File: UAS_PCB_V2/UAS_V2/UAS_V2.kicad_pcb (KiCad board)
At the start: 2 copper layers, 50.8 x 50.8 mm, 2 parts

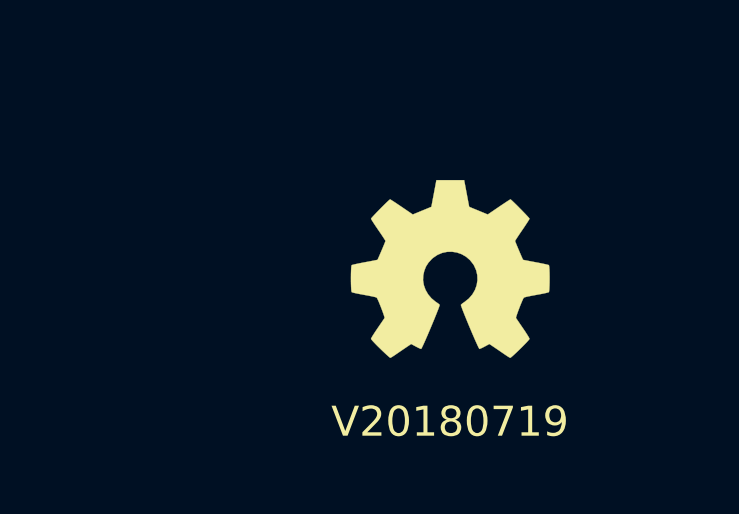
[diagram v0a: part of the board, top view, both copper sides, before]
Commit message: trace changes and fill for teensy pcb
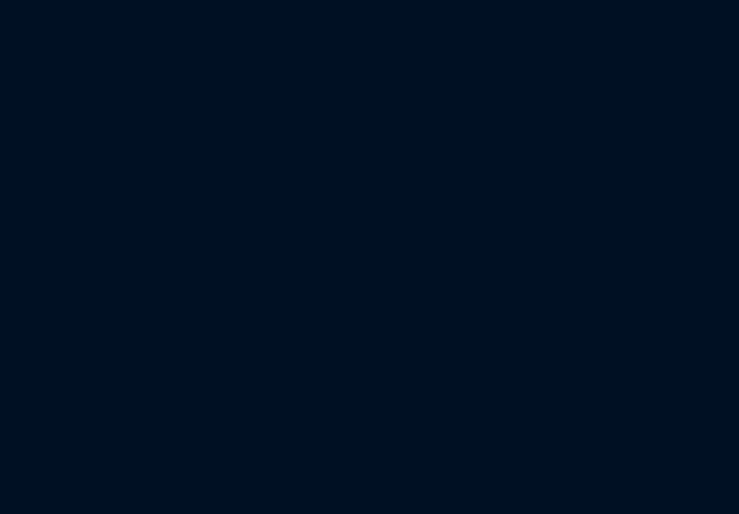
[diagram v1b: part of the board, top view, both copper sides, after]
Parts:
- removed N1: OHWLOGO, Symbols:OSHW-Symbol_6.7x6mm_SilkScreen
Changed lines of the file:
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@@
     (tracks 0)
     (zones 0)
-    (modules 2)
+    (modules 1)
     (nets 1)
   )
@@
     (uvia_drill 0.3)
   )
-  (module Symbols:OSHW-Symbol_6.7x6mm_SilkScreen (layer F.Cu)
-    (at 167.64 170.18)
-    (descr "Open Source Hardware Symbol")
-    (tags "Logo Symbol OSHW")
-    (attr virtual)
-    (fp_text reference N1 (at 0 -6.35) (layer F.SilkS) hide
-      (effects (font (size 1 1) (thickness 0.15)))
-    )
-    (fp_text value OHWLOGO (at 0 -8.89) (layer F.Fab) hide
-      (effects (font (size 1 1) (thickness 0.15)))
-    )
-    (fp_poly (pts (xy 0.555814 -2.531069) (xy 0.639635 -2.086445) (xy 0.94892 -1.958947) (xy 1.258206 -1.831449)
-      (xy 1.629246 -2.083754) (xy 1.733157 -2.154004) (xy 1.827087 -2.216728) (xy 1.906652 -2.269062)
-      (xy 1.96747 -2.308143) (xy 2.005157 -2.331107) (xy 2.015421 -2.336058) (xy 2.03391 -2.323324)
-      (xy 2.07342 -2.288118) (xy 2.129522 -2.234938) (xy 2.197787 -2.168282) (xy 2.273786 -2.092646)
-      (xy 2.353092 -2.012528) (xy 2.431275 -1.932426) (xy 2.503907 -1.856836) (xy 2.566559 -1.790255)
-      (xy 2.614803 -1.737182) (xy 2.64421 -1.702113) (xy 2.651241 -1.690377) (xy 2.641123 -1.66874)
-      (xy 2.612759 -1.621338) (xy 2.569129 -1.552807) (xy 2.513218 -1.467785) (xy 2.448006 -1.370907)
-      (xy 2.410219 -1.31565) (xy 2.341343 -1.214752) (xy 2.28014 -1.123701) (xy 2.229578 -1.04703)
-      (xy 2.192628 -0.989272) (xy 2.172258 -0.954957) (xy 2.169197 -0.947746) (xy 2.176136 -0.927252)
-      (xy 2.195051 -0.879487) (xy 2.223087 -0.811168) (xy 2.257391 -0.729011) (xy 2.295109 -0.63973)
-      (xy 2.333387 -0.550042) (xy 2.36937 -0.466662) (xy 2.400206 -0.396306) (xy 2.423039 -0.34569)
-      (xy 2.435017 -0.321529) (xy 2.435724 -0.320578) (xy 2.454531 -0.315964) (xy 2.504618 -0.305672)
-      (xy 2.580793 -0.290713) (xy 2.677865 -0.272099) (xy 2.790643 -0.250841) (xy 2.856442 -0.238582)
-      (xy 2.97695 -0.215638) (xy 3.085797 -0.193805) (xy 3.177476 -0.174278) (xy 3.246481 -0.158252)
-      (xy 3.287304 -0.146921) (xy 3.295511 -0.143326) (xy 3.303548 -0.118994) (xy 3.310033 -0.064041)
-      (xy 3.31497 0.015108) (xy 3.318364 0.112026) (xy 3.320218 0.220287) (xy 3.320538 0.333465)
-      (xy 3.319327 0.445135) (xy 3.31659 0.548868) (xy 3.312331 0.638241) (xy 3.306555 0.706826)
-      (xy 3.299267 0.748197) (xy 3.294895 0.75681) (xy 3.268764 0.767133) (xy 3.213393 0.781892)
-      (xy 3.136107 0.799352) (xy 3.04423 0.81778) (xy 3.012158 0.823741) (xy 2.857524 0.852066)
-      (xy 2.735375 0.874876) (xy 2.641673 0.89308) (xy 2.572384 0.907583) (xy 2.523471 0.919292)
-      (xy 2.490897 0.929115) (xy 2.470628 0.937956) (xy 2.458626 0.946724) (xy 2.456947 0.948457)
-      (xy 2.440184 0.976371) (xy 2.414614 1.030695) (xy 2.382788 1.104777) (xy 2.34726 1.191965)
-      (xy 2.310583 1.285608) (xy 2.275311 1.379052) (xy 2.243996 1.465647) (xy 2.219193 1.53874)
-      (xy 2.203454 1.591678) (xy 2.199332 1.617811) (xy 2.199676 1.618726) (xy 2.213641 1.640086)
-      (xy 2.245322 1.687084) (xy 2.291391 1.754827) (xy 2.348518 1.838423) (xy 2.413373 1.932982)
-      (xy 2.431843 1.959854) (xy 2.497699 2.057275) (xy 2.55565 2.146163) (xy 2.602538 2.221412)
-      (xy 2.635207 2.27792) (xy 2.6505 2.310581) (xy 2.651241 2.314593) (xy 2.638392 2.335684)
-      (xy 2.602888 2.377464) (xy 2.549293 2.435445) (xy 2.482171 2.505135) (xy 2.406087 2.582045)
-      (xy 2.325604 2.661683) (xy 2.245287 2.739561) (xy 2.169699 2.811186) (xy 2.103405 2.87207)
-      (xy 2.050969 2.917721) (xy 2.016955 2.94365) (xy 2.007545 2.947883) (xy 1.985643 2.937912)
-      (xy 1.9408 2.91102) (xy 1.880321 2.871736) (xy 1.833789 2.840117) (xy 1.749475 2.782098)
-      (xy 1.649626 2.713784) (xy 1.549473 2.645579) (xy 1.495627 2.609075) (xy 1.313371 2.4858)
-      (xy 1.160381 2.56852) (xy 1.090682 2.604759) (xy 1.031414 2.632926) (xy 0.991311 2.648991)
-      (xy 0.981103 2.651226) (xy 0.968829 2.634722) (xy 0.944613 2.588082) (xy 0.910263 2.515609)
-      (xy 0.867588 2.421606) (xy 0.818394 2.310374) (xy 0.76449 2.186215) (xy 0.707684 2.053432)
-      (xy 0.649782 1.916327) (xy 0.592593 1.779202) (xy 0.537924 1.646358) (xy 0.487584 1.522098)
-      (xy 0.44338 1.410725) (xy 0.407119 1.316539) (xy 0.380609 1.243844) (xy 0.365658 1.196941)
-      (xy 0.363254 1.180833) (xy 0.382311 1.160286) (xy 0.424036 1.126933) (xy 0.479706 1.087702)
-      (xy 0.484378 1.084599) (xy 0.628264 0.969423) (xy 0.744283 0.835053) (xy 0.83143 0.685784)
-      (xy 0.888699 0.525913) (xy 0.915086 0.359737) (xy 0.909585 0.191552) (xy 0.87119 0.025655)
-      (xy 0.798895 -0.133658) (xy 0.777626 -0.168513) (xy 0.666996 -0.309263) (xy 0.536302 -0.422286)
-      (xy 0.390064 -0.506997) (xy 0.232808 -0.562806) (xy 0.069057 -0.589126) (xy -0.096667 -0.58537)
-      (xy -0.259838 -0.55095) (xy -0.415935 -0.485277) (xy -0.560433 -0.387765) (xy -0.605131 -0.348187)
-      (xy -0.718888 -0.224297) (xy -0.801782 -0.093876) (xy -0.858644 0.052315) (xy -0.890313 0.197088)
-      (xy -0.898131 0.35986) (xy -0.872062 0.52344) (xy -0.814755 0.682298) (xy -0.728856 0.830906)
-      (xy -0.617014 0.963735) (xy -0.481877 1.075256) (xy -0.464117 1.087011) (xy -0.40785 1.125508)
-      (xy -0.365077 1.158863) (xy -0.344628 1.18016) (xy -0.344331 1.180833) (xy -0.348721 1.203871)
-      (xy -0.366124 1.256157) (xy -0.394732 1.33339) (xy -0.432735 1.431268) (xy -0.478326 1.545491)
-      (xy -0.529697 1.671758) (xy -0.585038 1.805767) (xy -0.642542 1.943218) (xy -0.700399 2.079808)
-      (xy -0.756802 2.211237) (xy -0.809942 2.333205) (xy -0.85801 2.441409) (xy -0.899199 2.531549)
-      (xy -0.931699 2.599323) (xy -0.953703 2.64043) (xy -0.962564 2.651226) (xy -0.98964 2.642819)
-      (xy -1.040303 2.620272) (xy -1.105817 2.587613) (xy -1.141841 2.56852) (xy -1.294832 2.4858)
-      (xy -1.477088 2.609075) (xy -1.570125 2.672228) (xy -1.671985 2.741727) (xy -1.767438 2.807165)
-      (xy -1.81525 2.840117) (xy -1.882495 2.885273) (xy -1.939436 2.921057) (xy -1.978646 2.942938)
-      (xy -1.991381 2.947563) (xy -2.009917 2.935085) (xy -2.050941 2.900252) (xy -2.110475 2.846678)
-      (xy -2.184542 2.777983) (xy -2.269165 2.697781) (xy -2.322685 2.646286) (xy -2.416319 2.554286)
-      (xy -2.497241 2.471999) (xy -2.562177 2.402945) (xy -2.607858 2.350644) (xy -2.631011 2.318616)
-      (xy -2.633232 2.312116) (xy -2.622924 2.287394) (xy -2.594439 2.237405) (xy -2.550937 2.167212)
-      (xy -2.495577 2.081875) (xy -2.43152 1.986456) (xy -2.413303 1.959854) (xy -2.346927 1.863167)
-      (xy -2.287378 1.776117) (xy -2.237984 1.703595) (xy -2.202075 1.650493) (xy -2.182981 1.621703)
-      (xy -2.181136 1.618726) (xy -2.183895 1.595782) (xy -2.198538 1.545336) (xy -2.222513 1.474041)
-      (xy -2.253266 1.388547) (xy -2.288244 1.295507) (xy -2.324893 1.201574) (xy -2.360661 1.113399)
-      (xy -2.392994 1.037634) (xy -2.419338 0.980931) (xy -2.437142 0.949943) (xy -2.438407 0.948457)
-      (xy -2.449294 0.939601) (xy -2.467682 0.930843) (xy -2.497606 0.921277) (xy -2.543103 0.909996)
-      (xy -2.608209 0.896093) (xy -2.696961 0.878663) (xy -2.813393 0.856798) (xy -2.961542 0.829591)
-      (xy -2.993618 0.823741) (xy -3.088686 0.805374) (xy -3.171565 0.787405) (xy -3.23493 0.771569)
-      (xy -3.271458 0.7596) (xy -3.276356 0.75681) (xy -3.284427 0.732072) (xy -3.290987 0.67679)
-      (xy -3.296033 0.597389) (xy -3.299559 0.500296) (xy -3.301561 0.391938) (xy -3.302036 0.27874)
-      (xy -3.300977 0.167128) (xy -3.298382 0.063529) (xy -3.294246 -0.025632) (xy -3.288563 -0.093928)
-      (xy -3.281331 -0.134934) (xy -3.276971 -0.143326) (xy -3.252698 -0.151792) (xy -3.197426 -0.165565)
-      (xy -3.116662 -0.18345) (xy -3.015912 -0.204252) (xy -2.900683 -0.226777) (xy -2.837902 -0.238582)
-      (xy -2.718787 -0.260849) (xy -2.612565 -0.281021) (xy -2.524427 -0.298085) (xy -2.459566 -0.311031)
-      (xy -2.423174 -0.318845) (xy -2.417184 -0.320578) (xy -2.407061 -0.34011) (xy -2.385662 -0.387157)
-      (xy -2.355839 -0.454997) (xy -2.320445 -0.536909) (xy -2.282332 -0.626172) (xy -2.244353 -0.716065)
-      (xy -2.20936 -0.799865) (xy -2.180206 -0.870853) (xy -2.159743 -0.922306) (xy -2.150823 -0.947503)
-      (xy -2.150657 -0.948604) (xy -2.160769 -0.968481) (xy -2.189117 -1.014223) (xy -2.232723 -1.081283)
-      (xy -2.288606 -1.165116) (xy -2.353787 -1.261174) (xy -2.391679 -1.31635) (xy -2.460725 -1.417519)
-      (xy -2.52205 -1.50937) (xy -2.572663 -1.587256) (xy -2.609571 -1.646531) (xy -2.629782 -1.682549)
-      (xy -2.632701 -1.690623) (xy -2.620153 -1.709416) (xy -2.585463 -1.749543) (xy -2.533063 -1.806507)
-      (xy -2.467384 -1.875815) (xy -2.392856 -1.952969) (xy -2.313913 -2.033475) (xy -2.234983 -2.112837)
-      (xy -2.1605 -2.18656) (xy -2.094894 -2.250148) (xy -2.042596 -2.299106) (xy -2.008039 -2.328939)
-      (xy -1.996478 -2.336058) (xy -1.977654 -2.326047) (xy -1.932631 -2.297922) (xy -1.865787 -2.254546)
-      (xy -1.781499 -2.198782) (xy -1.684144 -2.133494) (xy -1.610707 -2.083754) (xy -1.239667 -1.831449)
-      (xy -0.621095 -2.086445) (xy -0.537275 -2.531069) (xy -0.453454 -2.975693) (xy 0.471994 -2.975693)
-      (xy 0.555814 -2.531069)) (layer F.SilkS) (width 0.01))
-  )
   (module SquantorLabels:Label_version (layer F.Cu)
     (at 148 105)
@@
       (effects (font (size 1 1) (thickness 0.15)))
     )
-    (fp_text value V20180719 (at 19.64 70.26) (layer F.SilkS)
+    (fp_text value V20180719 (at 19.64 70.26) (layer F.SilkS) hide
       (effects (font (size 1 1) (thickness 0.15)))
     )

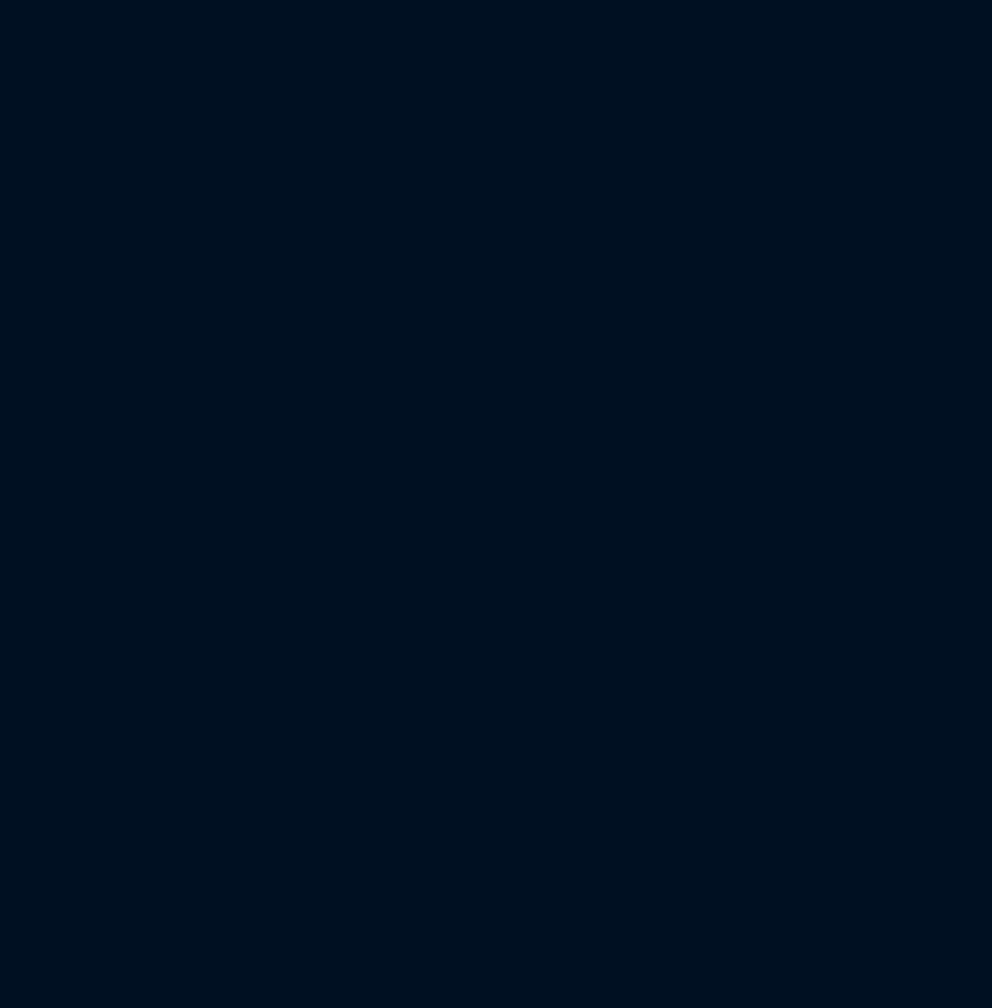
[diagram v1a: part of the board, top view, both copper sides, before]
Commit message: footprint file system fixes
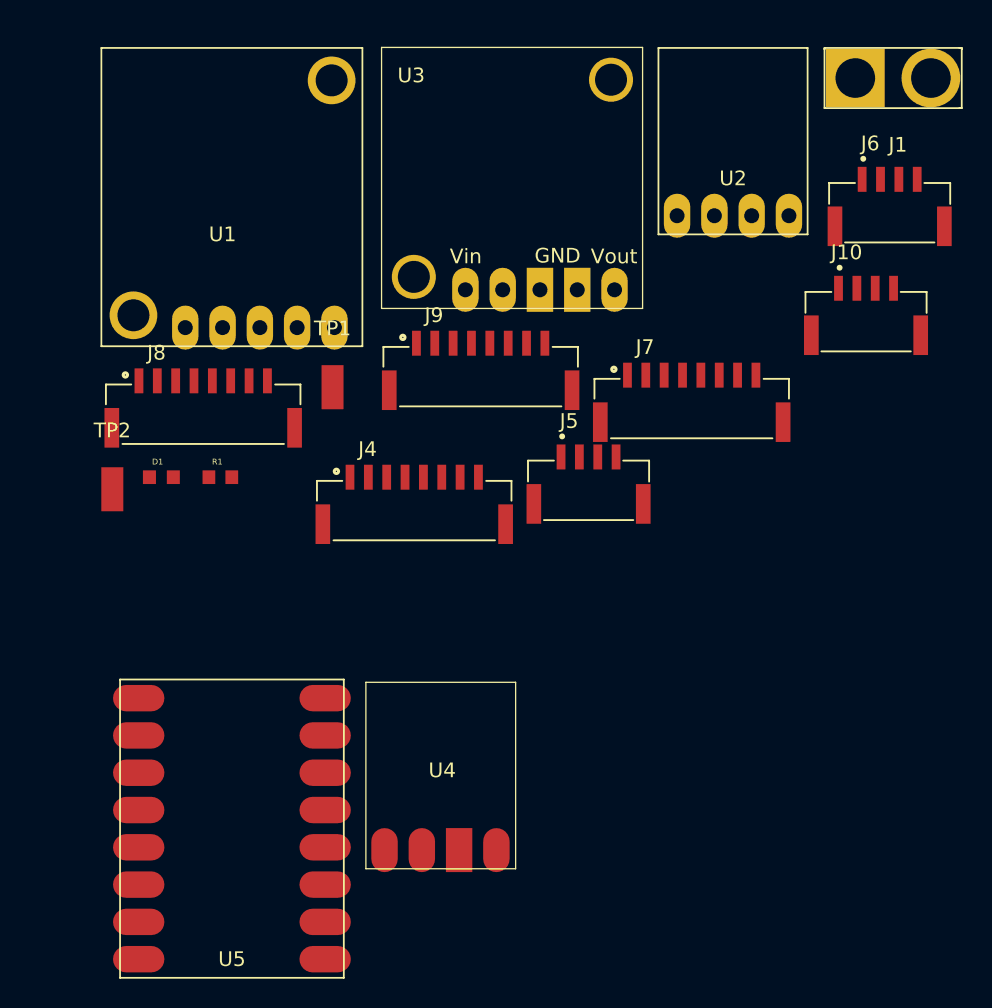
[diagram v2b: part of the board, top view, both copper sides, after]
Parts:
- added D1: Device_LED, UAS_V2:Indicator-LED, F.Cu at (188.0, 109.2)
- added J1: UAS_PWR_IN, UAS_V2:UAS_PCB_PWR_IN_PTOS, F.Cu at (238.1, 86.1)
- added J10: UAS_SM04B-GHS-TB(LF)(SN)-, UAS_V2:JST_SM04B-GHS-TB(LF)(SN)-, F.Cu at (236.0, 98.6)
- added J4: UAS_SM07B-GHS-TB(LF)(SN), UAS_V2:JST_SM08B-GHS-TB(LF)(SN), F.Cu at (205.2, 109.2)
- added J5: UAS_SM04B-GHS-TB(LF)(SN)-, UAS_V2:JST_SM04B-GHS-TB(LF)(SN)-, F.Cu at (217.1, 110.1)
- added J6: UAS_SM04B-GHS-TB(LF)(SN)-, UAS_V2:JST_SM04B-GHS-TB(LF)(SN)-, F.Cu at (237.6, 91.2)
- added J7: UAS_SM07B-GHS-TB(LF)(SN), UAS_V2:JST_SM08B-GHS-TB(LF)(SN), F.Cu at (224.1, 102.3)
- added J8: UAS_SM08B-GHS-TB(LF)(SN), UAS_V2:JST_SM08B-GHS-TB(LF)(SN), F.Cu at (190.8, 102.7)
- added J9: UAS_SM08B-GHS-TB(LF)(SN), UAS_V2:JST_SM08B-GHS-TB(LF)(SN), F.Cu at (209.7, 100.1)
- added R1: CR0603-JW-152ELF, UAS_V2:RESC1608X55N, F.Cu at (192.0, 109.2)
- added TP1: UAS-rescue_Signal-Pad-UAS-cache, UAS_V2:Individual_Solder_Pad, F.Cu at (199.6, 103.1)
- added TP2: UAS-rescue_Signal-Pad-UAS-cache, UAS_V2:Individual_Solder_Pad, F.Cu at (184.6, 110.0)
- added U1: UAS-rescue_5A-5V-Converter-UAS-cache, UAS_V2:Pololu_5V_5A_Step_Down_Regulator, F.Cu at (192.1, 90.1)
- added U2: UAS-rescue_500mA-5V-Converter-UAS-cache, UAS_V2:Pololu_5V_500mA_Step_Down_Regulator, F.Cu at (226.9, 86.3)
- added U3: 7.5V-2.5A-Step-Down(old), UAS_V2:Pololu_7.75V_2.5A_Step_Down_Regulator(old), F.Cu at (203.0, 97.7)
- added U4: 12V_500mA_Step_Up, UAS_V2:Pololu_12V_Step_Down_Regulator, F.Cu at (212.1, 123.2)
- added U5: UAS-rescue_TB6612FNG-Dual-Motor-Driver-UAS-cache, UAS_V2:Pololu_TB6612_Dual_Motor_Driver_Carrier_SMT, F.Cu at (192.8, 128.1)
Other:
- board text added: "Uh Oh Too Stinky"

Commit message: finalized merge
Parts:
- added J2: UAS_JST-3-pin-Revised-Symbol, UAS_V2:MOLEX_SHDRRA3W50P0X200_1X3_0353630360, B.Cu at (135.9, 120.7)
- added J3: UAS_JST-3-pin-Revised-Symbol, UAS_V2:MOLEX_SHDRRA3W50P0X200_1X3_0353630360, B.Cu at (167.6, 120.7)
- J10, J5, J6, J8, J9, U4: moved to B.Cu
- moved J6 110.0 mm to (127.6, 94.6), turned to 90 degrees
- moved J1 98.4 mm to (149.9, 129.5)
- moved U2 93.4 mm to (135.3, 104.1)
- moved J7 90.1 mm to (135.9, 83.8), turned to 180 degrees
- moved J5 89.6 mm to (127.6, 104.8), turned to 90 degrees
- moved J9 72.5 mm to (139.1, 83.8)
- moved TP1 66.7 mm to (137.2, 126.4)
- moved J10 63.3 mm to (172.7, 96.5), turned to 270 degrees
- moved U1 59.8 mm to (134.0, 104.1)
- moved TP2 56.2 mm to (130.8, 126.4)
- moved J8 52.9 mm to (138.9, 92.1)
- moved J4 48.5 mm to (163.8, 83.8), turned to 180 degrees
- moved U5 46.4 mm to (158.8, 96.5), turned to 90 degrees
- moved U3 46.4 mm to (157.5, 106.7), turned to 270 degrees
- moved R1 42.3 mm to (149.9, 113.0), turned to 180 degrees
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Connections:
- U5 pad 3: Net-(J10-Pad4) -> Net-(J10-Pad1)
- U5 pad 4: Net-(J10-Pad3) -> Net-(J10-Pad2)
- U5 pad 5: Net-(J10-Pad2) -> Net-(J10-Pad3)
- U5 pad 6: Net-(J10-Pad1) -> Net-(J10-Pad4)
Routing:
- net +5V: track 0.00 -> 109.6 mm, vias 0 -> 2
- net +24V: track 0.00 -> 55.1 mm
- net Net-(J3-Pad3): track 0.00 -> 34.4 mm
- net +7.5V: track 0.00 -> 34.4 mm
- net Net-(J10-Pad1): track 0.00 -> 16.8 mm, vias 0 -> 1
- net Net-(J7-Pad2): track 0.00 -> 13.8 mm, vias 0 -> 1
- net GND: track 0.00 -> 13.5 mm, vias 0 -> 5
- net Net-(J10-Pad2): track 0.00 -> 13.5 mm, vias 0 -> 1
- net Net-(J7-Pad1): track 0.00 -> 13.0 mm, vias 0 -> 1
- net Net-(J7-Pad5): track 0.00 -> 11.8 mm, vias 0 -> 1
- net Net-(J7-Pad4): track 0.00 -> 11.4 mm, vias 0 -> 1
- net Net-(J7-Pad3): track 0.00 -> 11.0 mm, vias 0 -> 1
- net Net-(J4-Pad6): track 0.00 -> 10.7 mm
- net Net-(J10-Pad3): track 0.00 -> 9.95 mm, vias 0 -> 1
- net +12V: track 0.00 -> 9.17 mm, vias 0 -> 1
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- added copper zone on B.Cu, net GND
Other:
- outline, holes or cut-outs redrawn
- board text added: "Created By: Bryce Derring"
- board text added: "GND"
- board text added: "JLCJLCJLCJLC"
- board text added: "UAS PCB Rev: 1.0 LBR - USLI 2020-2021 SERIAL NO."
- board text added: "Vin"
